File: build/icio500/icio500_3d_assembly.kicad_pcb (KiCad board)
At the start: 4 copper layers, 150.8 x 114.3 mm, 57 parts, among them J1 ?, U1 ?, U2 ?, U3 ?, U4 ?, U5 ?, U6 ?

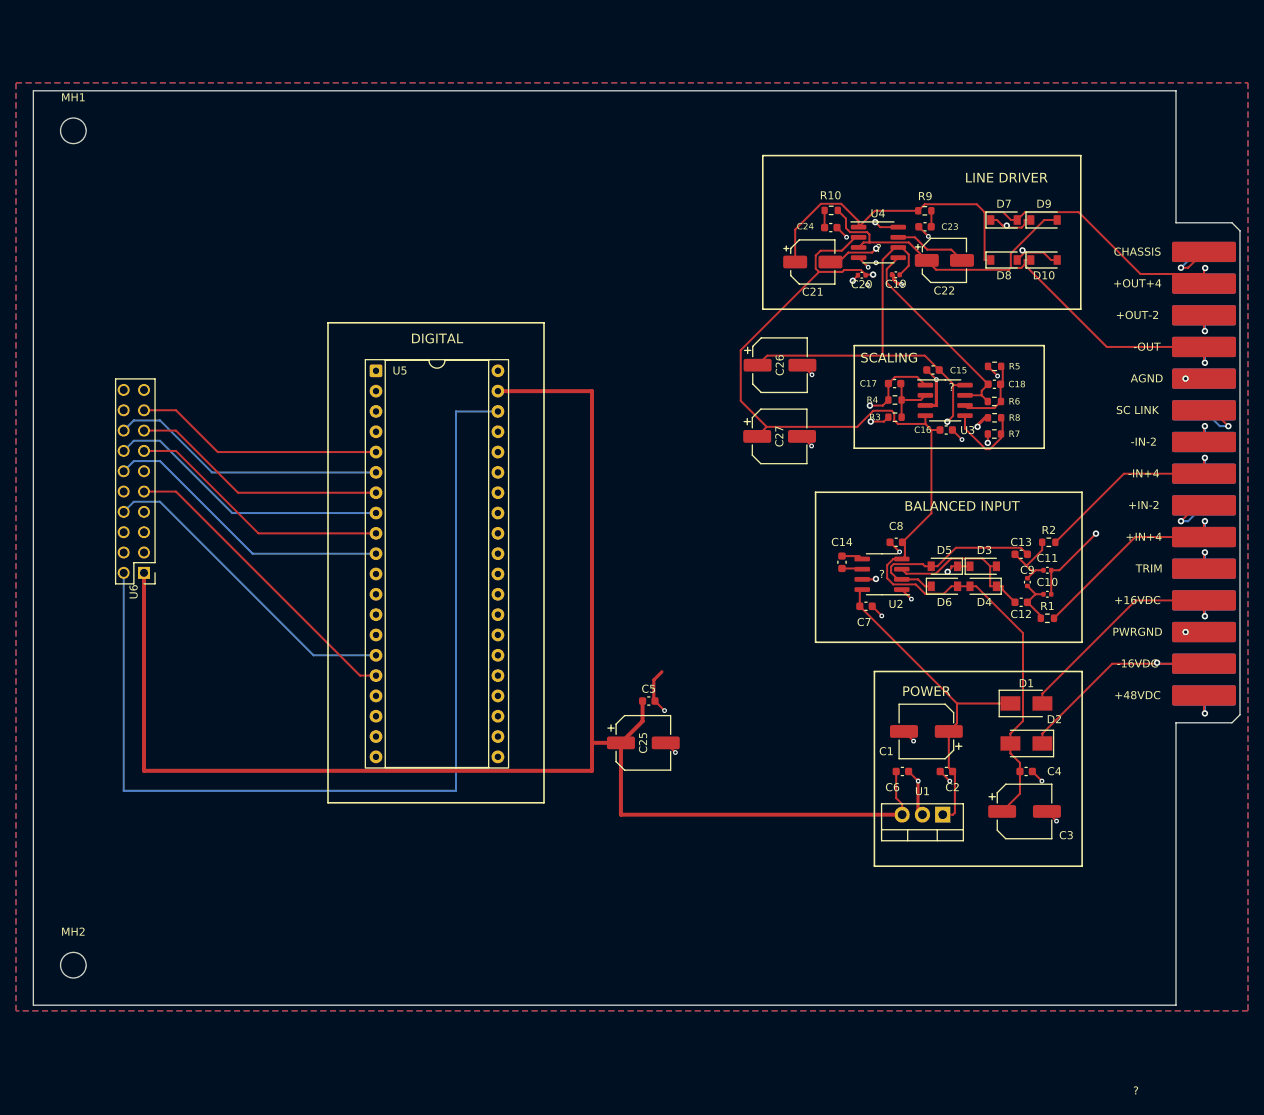
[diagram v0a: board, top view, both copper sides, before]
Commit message: Restore authentic VPR-500 carrier board outline (Y=55-160mm, 26mm notch) and concentric 3-point mating
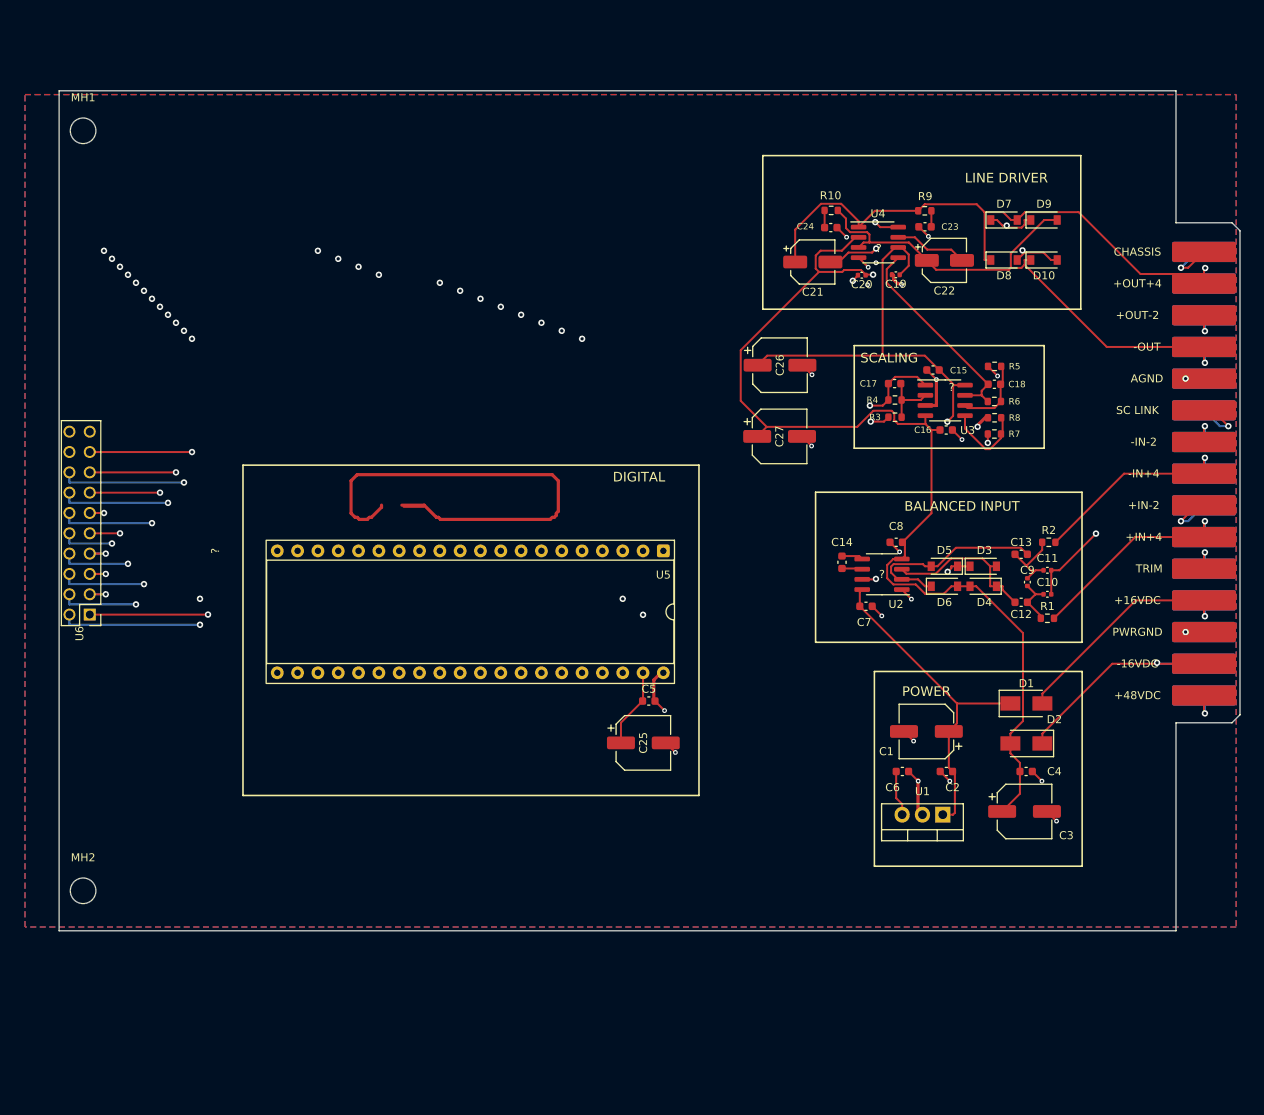
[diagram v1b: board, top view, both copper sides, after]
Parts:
- moved U5 42.4 mm to (130.9, 112.5), turned to -90 degrees
- moved MH2 9.38 mm to (58.4, 155.0)
- moved U6 8.55 mm to (59.2, 120.5)
- moved ? 3.22 mm to (55.4, 112.2)
- moved MH1 1.22 mm to (58.4, 60.0)
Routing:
- net i2c1_sda: track 34.8 -> 121.3 mm, vias 0 -> 3
- net i2c1_scl: track 34.8 -> 119.3 mm, vias 0 -> 3
- net spi1_mosi: track 36.9 -> 112.2 mm, vias 0 -> 3
- net spi1_sck: track 35.8 -> 110.7 mm, vias 0 -> 3
- net gnd: track 52.8 -> 127.7 mm, vias 25 -> 28
- net gpio_disp_dc: track 34.8 -> 109.3 mm, vias 0 -> 3
- net spi1_miso: track 33.3 -> 105.1 mm, vias 0 -> 3
- net spi1_cs: track 32.2 -> 103.7 mm, vias 0 -> 3
- net gpio_disp_res: track 31.2 -> 102.2 mm, vias 0 -> 3
- net d13: track 40.0 -> 110.6 mm, vias 0 -> 3
- net daisy_5v_power: track 199.8 -> 131.8 mm, vias 0 -> 2
- net d14: track 38.5 -> 102.4 mm, vias 0 -> 3
- net audio_in_r: track 121.4 -> 82.9 mm, vias 0 -> 3
- net gpio_enc_b: track 69.0 -> 107.0 mm, vias 0 -> 3
- net gpio_enc_sw: track 80.4 -> 98.8 mm, vias 0 -> 3
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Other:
- board size 150.8 x 114.3 mm -> 147.6 x 105 mm

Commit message: Fix VPR-500 carrier edge cuts, center card tongue with zero bottom bulk, and align U6 header mating to 0.000mm
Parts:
- moved U6 11.4 mm to (59.2, 131.9)
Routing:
- net spi1_sck: track 110.7 -> 122.2 mm
- net spi1_miso: track 105.1 -> 116.6 mm
- net spi1_cs: track 103.7 -> 115.1 mm
- net gpio_enc_b: track 107.0 -> 118.4 mm
- net d14: track 102.4 -> 113.9 mm
- net d13: track 110.6 -> 122.0 mm
- net audio_in_r: track 82.9 -> 94.4 mm
- net gpio_enc_sw: track 98.8 -> 110.2 mm
- net gpio_disp_res: track 102.2 -> 113.6 mm
- net spi1_mosi: track 112.2 -> 123.6 mm
- net i2c1_sda: track 121.3 -> 132.7 mm
- net i2c1_scl: track 119.3 -> 130.7 mm
- net gpio_disp_dc: track 109.3 -> 120.7 mm
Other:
- board size 147.6 x 105 mm -> 147.6 x 114.3 mm

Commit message: Restore authentic UI faceplate with complete VU meter, dial markings, and encoder hole; resolve carrier 5V trace and achieve 0 DRC violations across all boards
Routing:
- net daisy_5v_power: track 131.8 -> 143.2 mm
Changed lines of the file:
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@@
 	)
 	(segment
-		(start 59.22 131.905) (end 74.0 131.905)
+		(start 59.22 131.905)
+		(end 74 131.905)
 		(width 0.25)
 		(layer "F.Cu")
@@
 	)
 	(via
-		(at 74.0 131.905)
+		(at 74 131.905)
 		(size 0.8)
 		(drill 0.4)
@@
 	)
 	(segment
+		(start 74 131.905)
+		(end 74 120.5)
+		(width 0.25)
+		(layer "In1.Cu")
+		(net "daisy_5v_power")
+	)
+	(segment
 		(start 74 120.5)
 		(end 128.38 120.5)
@@
 	)
 	(segment
-		(start 74.0 131.905) (end 74.0 131.905)
+		(start 74 131.905)
+		(end 74 131.905)
 		(width 0.25)
 		(layer "In2.Cu")
@@
 	)
 	(segment
-		(start 59.22 124.285) (end 61.22 124.285)
+		(start 59.22 124.285)
+		(end 61.22 124.285)
 		(width 0.25)
 		(layer "F.Cu")
@@
 	)
 	(segment
-		(start 59.22 126.825) (end 61.22 126.825)
+		(start 59.22 126.825)
+		(end 61.22 126.825)
 		(width 0.25)
 		(layer "F.Cu")
@@
 	)
 	(segment
-		(start 59.22 129.365) (end 61.22 129.365)
+		(start 59.22 129.365)
+		(end 61.22 129.365)
 		(width 0.25)
 		(layer "F.Cu")
@@
 	)
 	(segment
-		(start 59.22 126.825) (end 61.22 126.825)
+		(start 59.22 126.825)
+		(end 61.22 126.825)
 		(width 0.25)
 		(layer "B.Cu")
@@
 	)
 	(segment
-		(start 59.22 124.285) (end 61.22 124.285)
+		(start 59.22 124.285)
+		(end 61.22 124.285)
 		(width 0.25)
 		(layer "B.Cu")
@@
 	)
 	(segment
-		(start 59.22 129.365) (end 61.22 129.365)
+		(start 59.22 129.365)
+		(end 61.22 129.365)
 		(width 0.25)
 		(layer "B.Cu")
@@
 	)
 	(segment
-		(start 59.22 111.585) (end 72.0 111.585)
+		(start 59.22 111.585)
+		(end 72 111.585)
 		(width 0.25)
 		(layer "F.Cu")
@@
 	)
 	(via
-		(at 72.0 111.585)
+		(at 72 111.585)
 		(size 0.8)
 		(drill 0.4)
@@
 	)
 	(segment
-		(start 72.0 111.585)
+		(start 72 111.585)
 		(end 72 86)
 		(width 0.25)
@@
 	)
 	(via
-		(at 71.0 115.395)
+		(at 71 115.395)
 		(size 0.8)
 		(drill 0.4)
@@
 	)
 	(segment
-		(start 56.68 114.125) (end 56.68 115.395)
+		(start 56.68 114.125)
+		(end 56.68 115.395)
 		(width 0.25)
 		(layer "B.Cu")
@@
 	)
 	(segment
-		(start 56.68 115.395) (end 71.0 115.395)
+		(start 56.68 115.395)
+		(end 71 115.395)
 		(width 0.25)
 		(layer "B.Cu")
@@
 	)
 	(segment
-		(start 71.0 115.395)
+		(start 71 115.395)
 		(end 71 85)
 		(width 0.25)
@@
 	)
 	(segment
-		(start 59.22 114.125) (end 70.0 114.125)
+		(start 59.22 114.125)
+		(end 70 114.125)
 		(width 0.25)
 		(layer "F.Cu")
@@
 	)
 	(via
-		(at 70.0 114.125)
+		(at 70 114.125)
 		(size 0.8)
 		(drill 0.4)
@@
 	)
 	(segment
-		(start 70.0 114.125)
+		(start 70 114.125)
 		(end 70 84)
 		(width 0.25)
@@
 	)
 	(via
-		(at 69.0 117.935)
+		(at 69 117.935)
 		(size 0.8)
 		(drill 0.4)
@@
 	)
 	(segment
-		(start 56.68 116.665) (end 56.68 117.935)
+		(start 56.68 116.665)
+		(end 56.68 117.935)
 		(width 0.25)
 		(layer "B.Cu")
@@
 	)
 	(segment
-		(start 56.68 117.935) (end 69.0 117.935)
+		(start 56.68 117.935)
+		(end 69 117.935)
 		(width 0.25)
 		(layer "B.Cu")
@@
 	)
 	(segment
-		(start 69.0 117.935)
+		(start 69 117.935)
 		(end 69 83)
 		(width 0.25)
@@
 	)
 	(segment
-		(start 59.22 116.665) (end 68.0 116.665)
+		(start 59.22 116.665)
+		(end 68 116.665)
 		(width 0.25)
 		(layer "F.Cu")
@@
 	)
 	(via
-		(at 68.0 116.665)
+		(at 68 116.665)
 		(size 0.8)
 		(drill 0.4)
@@
 	)
 	(segment
-		(start 68.0 116.665)
+		(start 68 116.665)
 		(end 68 82)
 		(width 0.25)
@@
 	)
 	(via
-		(at 67.0 120.475)
+		(at 67 120.475)
 		(size 0.8)
 		(drill 0.4)
@@
 	)
 	(segment
-		(start 56.68 119.205) (end 56.68 120.475)
+		(start 56.68 119.205)
+		(end 56.68 120.475)
 		(width 0.25)
 		(layer "B.Cu")
@@
 	)
 	(segment
-		(start 56.68 120.475) (end 67.0 120.475)
+		(start 56.68 120.475)
+		(end 67 120.475)
 		(width 0.25)
 		(layer "B.Cu")
@@
 	)
 	(segment
-		(start 67.0 120.475)
+		(start 67 120.475)
 		(end 67 81)
 		(width 0.25)
@@
 	)
 	(via
-		(at 66.0 128.095)
+		(at 66 128.095)
 		(size 0.8)
 		(drill 0.4)
@@
 	)
 	(segment
-		(start 56.68 128.095) (end 66.0 128.095)
+		(start 56.68 128.095)
+		(end 66 128.095)
 		(width 0.25)
 		(layer "B.Cu")
@@
 	)
 	(segment
-		(start 56.68 126.825) (end 56.68 128.095)
+		(start 56.68 126.825)
+		(end 56.68 128.095)
 		(width 0.25)
 		(layer "B.Cu")
@@
 	)
 	(segment
-		(start 66.0 128.095)
+		(start 66 128.095)
 		(end 66 80)
 		(width 0.25)
@@
 	)
 	(via
-		(at 65.0 130.635)
+		(at 65 130.635)
 		(size 0.8)
 		(drill 0.4)
@@
 	)
 	(segment
-		(start 56.68 130.635) (end 65.0 130.635)
+		(start 56.68 130.635)
+		(end 65 130.635)
 		(width 0.25)
 		(layer "B.Cu")
@@
 	)
 	(segment
-		(start 56.68 129.365) (end 56.68 130.635)
+		(start 56.68 129.365)
+		(end 56.68 130.635)
 		(width 0.25)
 		(layer "B.Cu")
@@
 	)
 	(segment
-		(start 65.0 130.635)
+		(start 65 130.635)
 		(end 65 79)
 		(width 0.25)
@@
 	)
 	(via
-		(at 64.0 125.555)
+		(at 64 125.555)
 		(size 0.8)
 		(drill 0.4)
@@
 	)
 	(segment
-		(start 56.68 124.285) (end 56.68 125.555)
+		(start 56.68 124.285)
+		(end 56.68 125.555)
 		(width 0.25)
 		(layer "B.Cu")
@@
 	)
 	(segment
-		(start 56.68 125.555) (end 64.0 125.555)
+		(start 56.68 125.555)
+		(end 64 125.555)
 		(width 0.25)
 		(layer "B.Cu")
@@
 	)
 	(segment
-		(start 64.0 125.555)
+		(start 64 125.555)
 		(end 64 78)
 		(width 0.25)
@@
 	)
 	(segment
-		(start 59.22 121.745) (end 63.0 121.745)
+		(start 59.22 121.745)
+		(end 63 121.745)
 		(width 0.25)
 		(layer "F.Cu")
@@
 	)
 	(via
-		(at 63.0 121.745)
+		(at 63 121.745)
 		(size 0.8)
 		(drill 0.4)
@@
 	)
 	(segment
-		(start 63.0 121.745)
+		(start 63 121.745)
 		(end 63 77)
 		(width 0.25)
@@
 	)
 	(via
-		(at 62.0 123.015)
+		(at 62 123.015)
 		(size 0.8)
 		(drill 0.4)
@@
 	)
 	(segment
-		(start 56.68 123.015) (end 62.0 123.015)
+		(start 56.68 123.015)
+		(end 62 123.015)
 		(width 0.25)
 		(layer "B.Cu")
@@
 	)
 	(segment
-		(start 56.68 121.745) (end 56.68 123.015)
+		(start 56.68 121.745)
+		(end 56.68 123.015)
 		(width 0.25)
 		(layer "B.Cu")
@@
 	)
 	(segment
-		(start 62.0 123.015)
+		(start 62 123.015)
 		(end 62 76)
 		(width 0.25)
@@
 	)
 	(segment
-		(start 59.22 119.205) (end 61.0 119.205)
+		(start 59.22 119.205)
+		(end 61 119.205)
 		(width 0.25)
 		(layer "F.Cu")
@@
 	)
 	(via
-		(at 61.0 119.205)
+		(at 61 119.205)
 		(size 0.8)
 		(drill 0.4)
@@
 	)
 	(segment
-		(start 61.0 119.205)
+		(start 61 119.205)
 		(end 61 75)
 		(width 0.25)
@@
 	)
 	(via
-		(at 73.0 133.175)
+		(at 73 133.175)
 		(size 0.8)
 		(drill 0.4)
@@
 	)
 	(segment
-		(start 56.68 133.175) (end 73.0 133.175)
+		(start 56.68 133.175)
+		(end 73 133.175)
 		(width 0.25)
 		(layer "B.Cu")
@@
 	)
 	(segment
-		(start 56.68 131.905) (end 56.68 133.175)
+		(start 56.68 131.905)
+		(end 56.68 133.175)
 		(width 0.25)
 		(layer "B.Cu")
@@
 	)
 	(segment
-		(start 73.0 133.175)
+		(start 73 133.175)
 		(end 73 118.5)
 		(width 0.25)
@@
 		(polygon
 			(pts
-				(xy 49.625 44.0) (xy 204.025 44.0) (xy 204.025 161.025) (xy 49.625 161.025)
+				(xy 49.625 44) (xy 204.025 44) (xy 204.025 161.025) (xy 49.625 161.025)
 			)
 		)

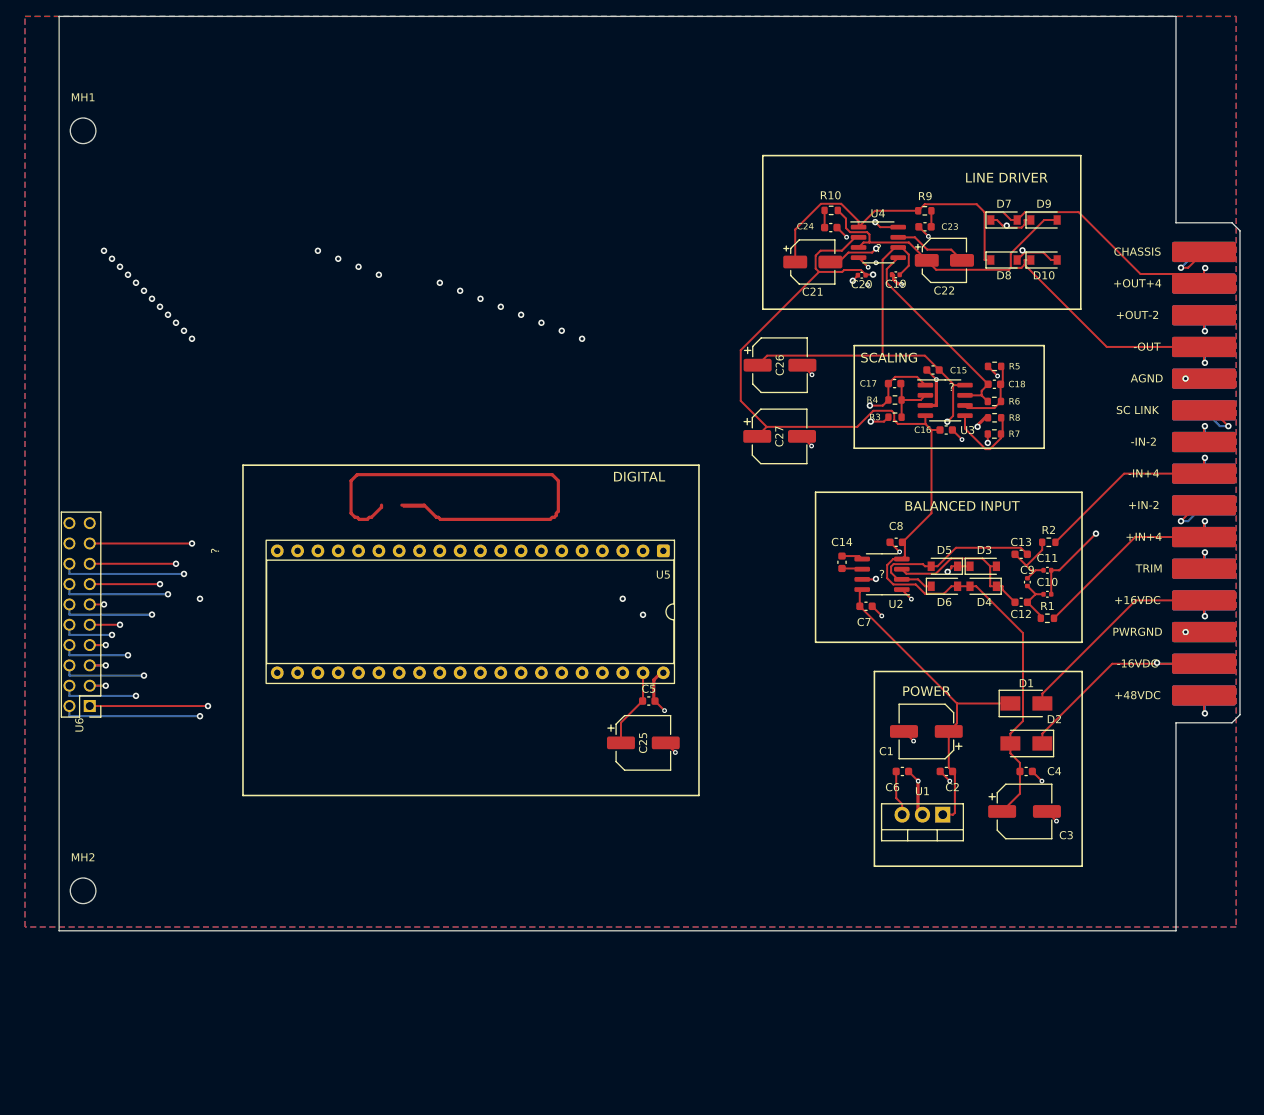
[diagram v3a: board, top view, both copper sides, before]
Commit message: Restore vertical Daisy Seed (U5 at 95,90), strip all words from faceplate leaving only right-side level indicators, center tongue with zero bottom bulk, and verify 0 DRC violations
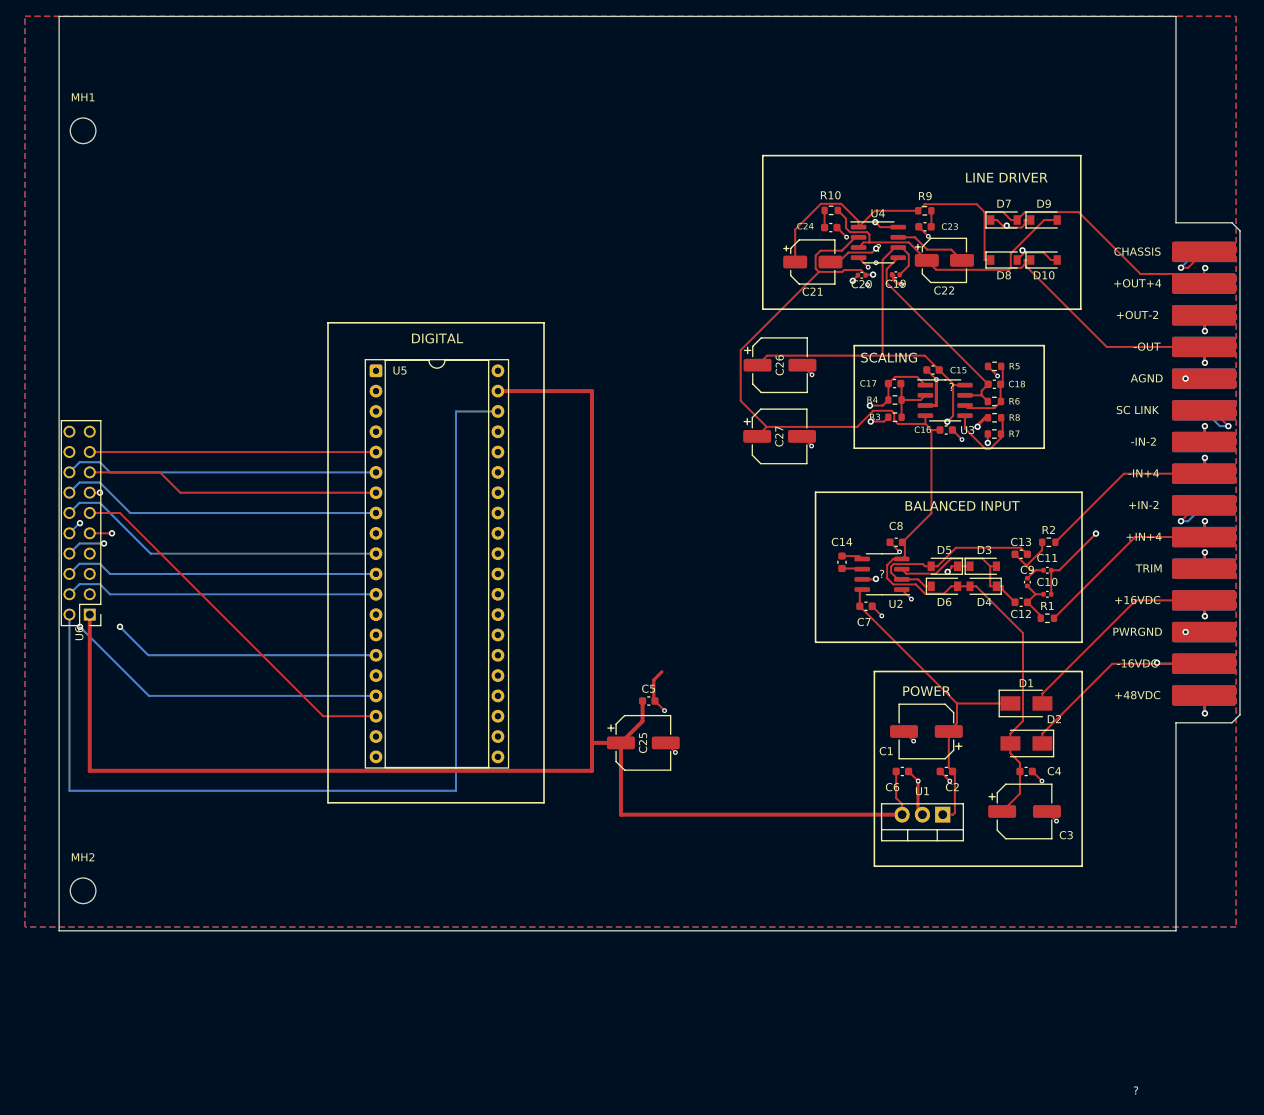
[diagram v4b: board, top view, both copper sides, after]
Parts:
- removed the ? at (55.4, 112.2)
- added ?: , DUMMY, F.Cu at (55.4, 112.2)
- moved U5 42.4 mm to (95.0, 90.0), turned to 0 degrees
- moved U6 11.4 mm to (59.2, 120.5)
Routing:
- net i2c1_sda: track 132.7 -> 39.4 mm, vias 3 -> 0
- net i2c1_scl: track 130.7 -> 39.4 mm, vias 3 -> 0
- net spi1_mosi: track 123.6 -> 41.5 mm, vias 3 -> 0
- net spi1_sck: track 122.2 -> 40.4 mm, vias 3 -> 0
- net gpio_disp_dc: track 120.7 -> 39.4 mm, vias 3 -> 0
- net spi1_miso: track 116.6 -> 37.9 mm, vias 3 -> 1
- net spi1_cs: track 115.1 -> 36.8 mm, vias 3 -> 0
- net gpio_disp_res: track 113.6 -> 35.8 mm, vias 3 -> 0
- net gnd: track 127.7 -> 52.8 mm, vias 28 -> 25
- net d13: track 122.0 -> 50.7 mm, vias 3 -> 2
- net d14: track 113.9 -> 47.6 mm, vias 3 -> 1
- net gpio_enc_sw: track 110.2 -> 46.3 mm, vias 3 -> 0
- net gpio_enc_b: track 118.4 -> 55.4 mm, vias 3 -> 2
- net daisy_5v_power: track 143.2 -> 201.3 mm, vias 2 -> 0
- net audio_in_r: track 94.4 -> 123.0 mm, vias 3 -> 0
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
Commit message: Align 500-series chassis rail mounting: center faceplate on card tongue (Y=102.75mm), restore Würth SMD brackets in 3D assembly, and confirm 0 DRC violations
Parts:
- moved ? 9.40 mm to (55.4, 102.8)
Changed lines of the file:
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@@
 	(footprint "DUMMY"
 		(layer "F.Cu")
-		(at 55.39 112.15)
+		(at 55.39 102.75)
 		(attr exclude_from_pos_files exclude_from_bom)
 		(model "C:/Users/Chris Williams/Documents/GitHub/ICIO500/build/icio500/panel_satellite.step"
-			(offset (xyz -0.08 166.675 -108.74))
+			(offset (xyz -105.24 166.675 0.0))
 			(scale (xyz 1 1 1))
 			(rotate (xyz 0 90 0))
 		)
 		(model "C:/Users/Chris Williams/Documents/GitHub/ICIO500/build/icio500/faceplate_front.step"
-			(offset (xyz -1.68 66.675 -8.74))
+			(offset (xyz -5.24 66.675 -1.6))
 			(scale (xyz 1 1 1))
 			(rotate (xyz 0 90 0))
